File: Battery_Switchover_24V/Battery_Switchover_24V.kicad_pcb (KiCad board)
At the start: 4 copper layers, 198.6 x 89 mm, 186 parts, among them J1 USB_C_Receptacle_USB2.0_14P, J10 ATX_2X3, J11 ATX_2X3, J12 ATX_2X3, J13 ATX_2X3, J2 M8, J4 M8, J5 M8, J6 Conn_01x08, J7 Conn_01x05, J8 ATX_2X3, J9 ATX_2X3, M1 Fan, Q1 PZT2222AT1G, Q10 FDBL86066-F085, Q11 BC817, Q2 PJD50N10AL_L2, Q3 PJD50N10AL_L2, Q4 FDBL86066-F085, Q5 FDBL86066-F085, Q6 FDBL86066-F085, Q7 FDBL86066-F085, Q8 FDBL86066-F085, Q9 FDBL86066-F085, SW1 SW_Push, SW2 SW_Push, SW3 SW_Push, U1 LM25117PSQE_NOPB, U10 LPC11U67JBD48, U12 L5973D, U13 AMS1117-3.3, U14 OPA2197xD, U15 IRS21867S, U16 LM74610QDGKRQ1, U17 IRS21867S, U18 LM60CIM3_NOPB, U2 ACS71240LLCBTR-010B3, U3 IRS21867S, U4 ACS71240LLCBTR-010B3, U5 ACS71240LLCBTR-010B3, U6 LM74610QDGKRQ1, U7 ACS71240LLCBTR-010B3, U8 ADS7830IPWR, U9 LMV321

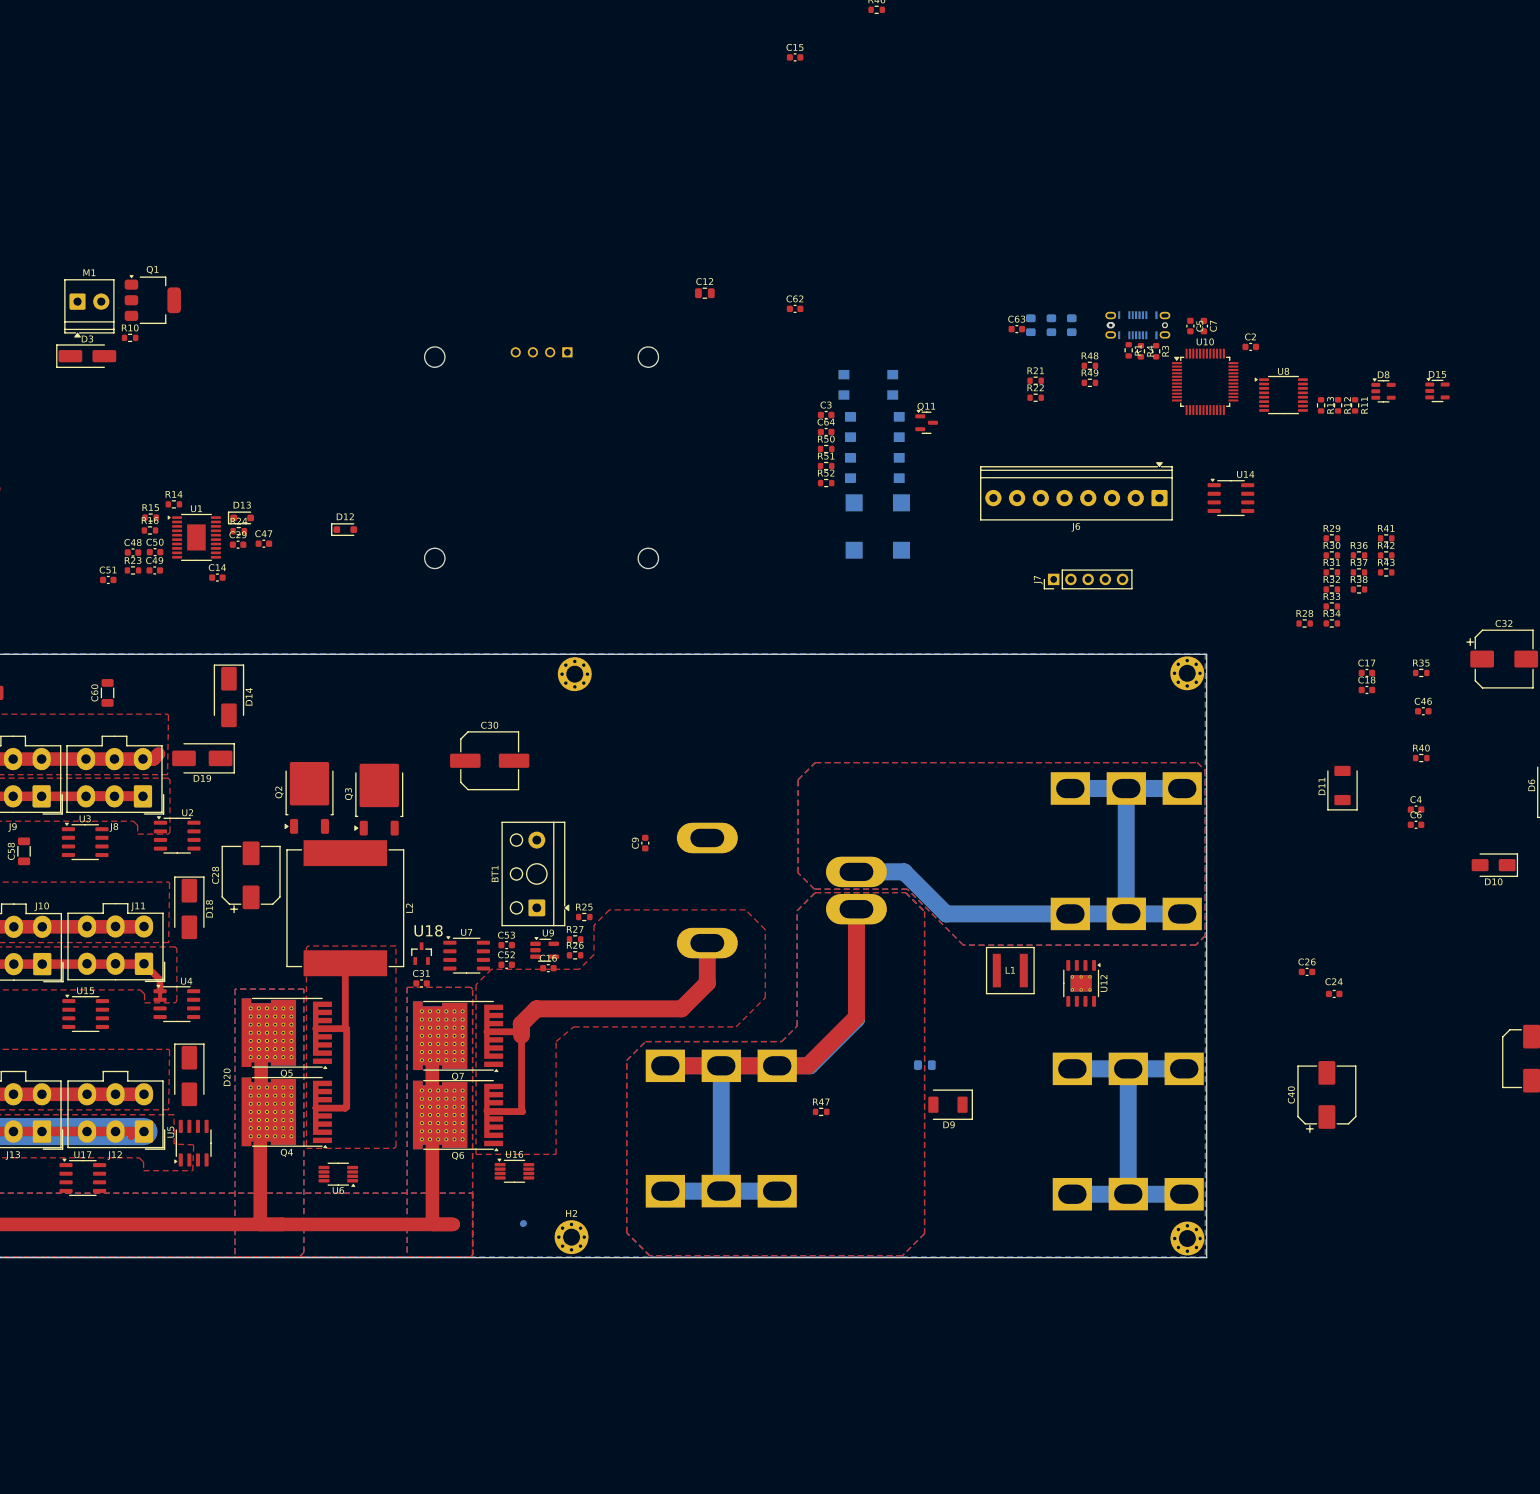
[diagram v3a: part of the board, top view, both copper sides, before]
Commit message: Added batt terminals
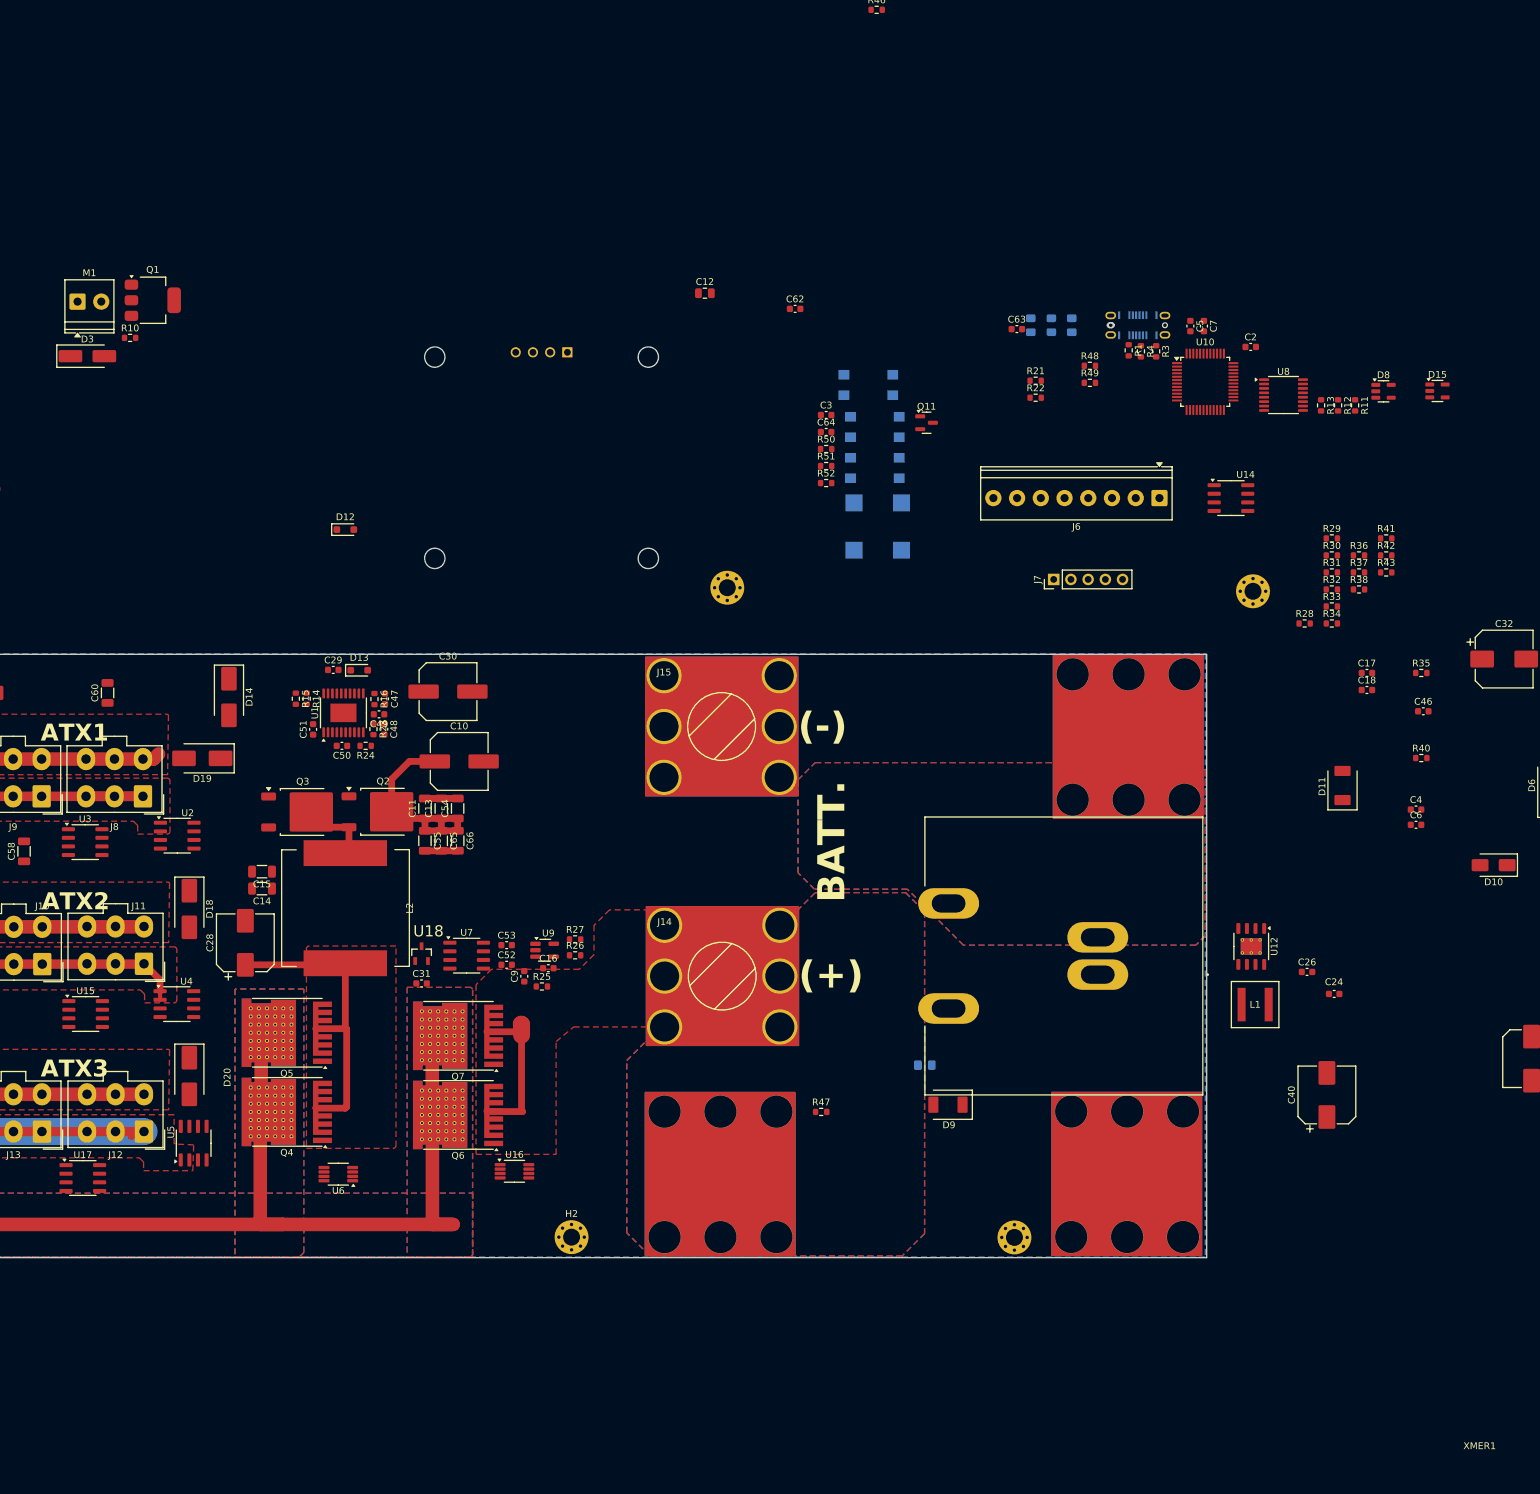
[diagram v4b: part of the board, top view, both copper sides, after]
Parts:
- removed BT1: Battery_Cell, TerminalBlock_RND:TerminalBlock_RND_205-00023_1x02_P10.00mm_Horizontal
- added C10: 330uF, Capacitor_SMD:C_Elec_8x10.2, F.Cu at (177.6, 85.8)
- added C11: 10uF 50V X7R, Capacitor_SMD:C_1206_3216Metric, F.Cu at (172.6, 92.7)
- added C13: 10uF 50V X7R, Capacitor_SMD:C_1206_3216Metric, F.Cu at (175.0, 92.7)
- added C54: 10uF 50V X7R, Capacitor_SMD:C_1206_3216Metric, F.Cu at (177.4, 92.7)
- added C55: 10uF 50V X7R, Capacitor_SMD:C_1206_3216Metric, F.Cu at (172.6, 97.5)
- added C65: 10uF 50V X7R, Capacitor_SMD:C_1206_3216Metric, F.Cu at (174.9, 97.5)
- added C66: 10uF 50V X7R, Capacitor_SMD:C_1206_3216Metric, F.Cu at (177.4, 97.5)
- added J14: M6, M8_Screw_Terminal:M6_Screw_Terminal, F.Cu at (207.9, 110.0)
- added J15: M6, M8_Screw_Terminal:M6_Screw_Terminal, F.Cu at (207.8, 73.2)
- C14: value 100nF -> 10uF; footprint Capacitor_SMD:C_0603_1608Metric -> Capacitor_SMD:C_1206_3216Metric
- C15: footprint Capacitor_SMD:C_0603_1608Metric -> Capacitor_SMD:C_1206_3216Metric
- L2: value L -> 8.2uH 20A
- XMER1: moved to F.Cu
- moved C15 143.6 mm to (148.5, 102.1), turned to 180 degrees
- moved C14 46.3 mm to (148.5, 104.6), turned to 180 degrees
- moved C48 45.3 mm to (166.6, 81.0), turned to -90 degrees
- moved R23 42.5 mm to (164.9, 81.0), turned to -90 degrees
- moved R16 41.4 mm to (165.1, 76.6), turned to -90 degrees
- moved C50 39.7 mm to (160.3, 83.5), turned to 180 degrees
- moved C49 39.3 mm to (165.8, 78.8), turned to 180 degrees
- moved C51 37.4 mm to (156.1, 81.1), turned to 90 degrees
- moved XMER1 36.9 mm to (266.8, 114.5)
- moved R24 36.8 mm to (163.8, 83.5), turned to 180 degrees
- moved L1 36.5 mm to (295.0, 121.7)
- moved R14 34.7 mm to (155.1, 76.5), turned to -90 degrees
- moved R15 34.2 mm to (153.5, 76.5), turned to -90 degrees
- moved U1 33.8 mm to (160.5, 78.6), turned to 90 degrees
- moved C47 29.0 mm to (166.7, 76.6), turned to -90 degrees
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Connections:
- C14 pad 1: VBATT -> Net-(U7-IP+1)
- C15 pad 1: VBATT -> Net-(U7-IP+1)
- C28 pad 1: VBATT -> Net-(U7-IP+1)
- L2 pad 2: VBATT -> Net-(U7-IP+1)
- U7 pad 1: Net-(BT1--) -> Net-(U7-IP+1)
- U7 pad 2: Net-(BT1--) -> Net-(U7-IP+1)
- U7 pad 3: GND -> VBATT
- U7 pad 4: GND -> VBATT
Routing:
- net Net-(D6-A1): track 85.6 -> 0.00 mm
- net Net-(D16-K): track 129.4 -> 51.5 mm
- net VBATT: track 30.5 -> 45.4 mm
- net Net-(Q2-S): track 0.00 -> 10.5 mm
- net GND: track 0.00 -> 9.65 mm
- net VIN: track 59.8 -> 56.7 mm
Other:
- board text added: "(+)"
- board text added: "(-)"
- board text added: "ATX1"
- board text added: "ATX2"
- board text added: "ATX3"
- board text added: "BATT."

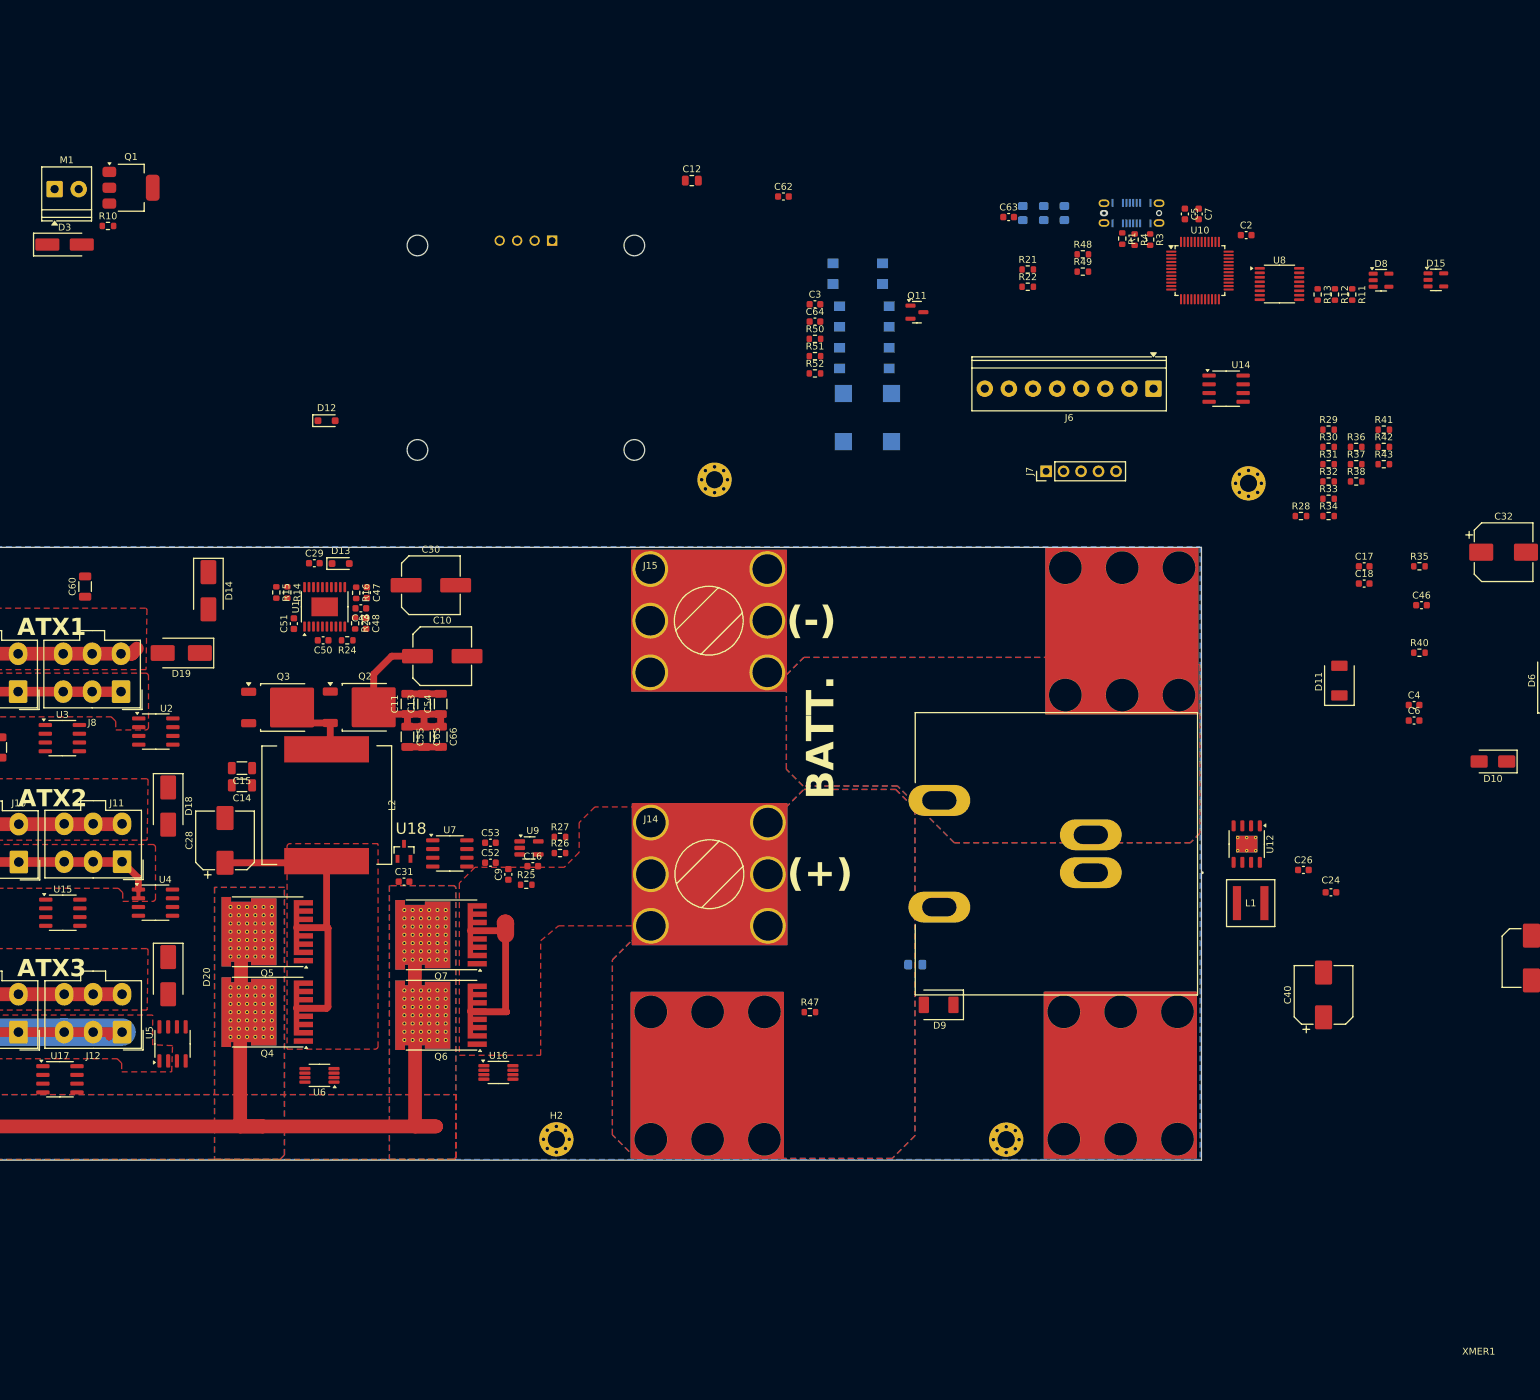
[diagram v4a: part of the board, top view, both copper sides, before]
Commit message: keep outs
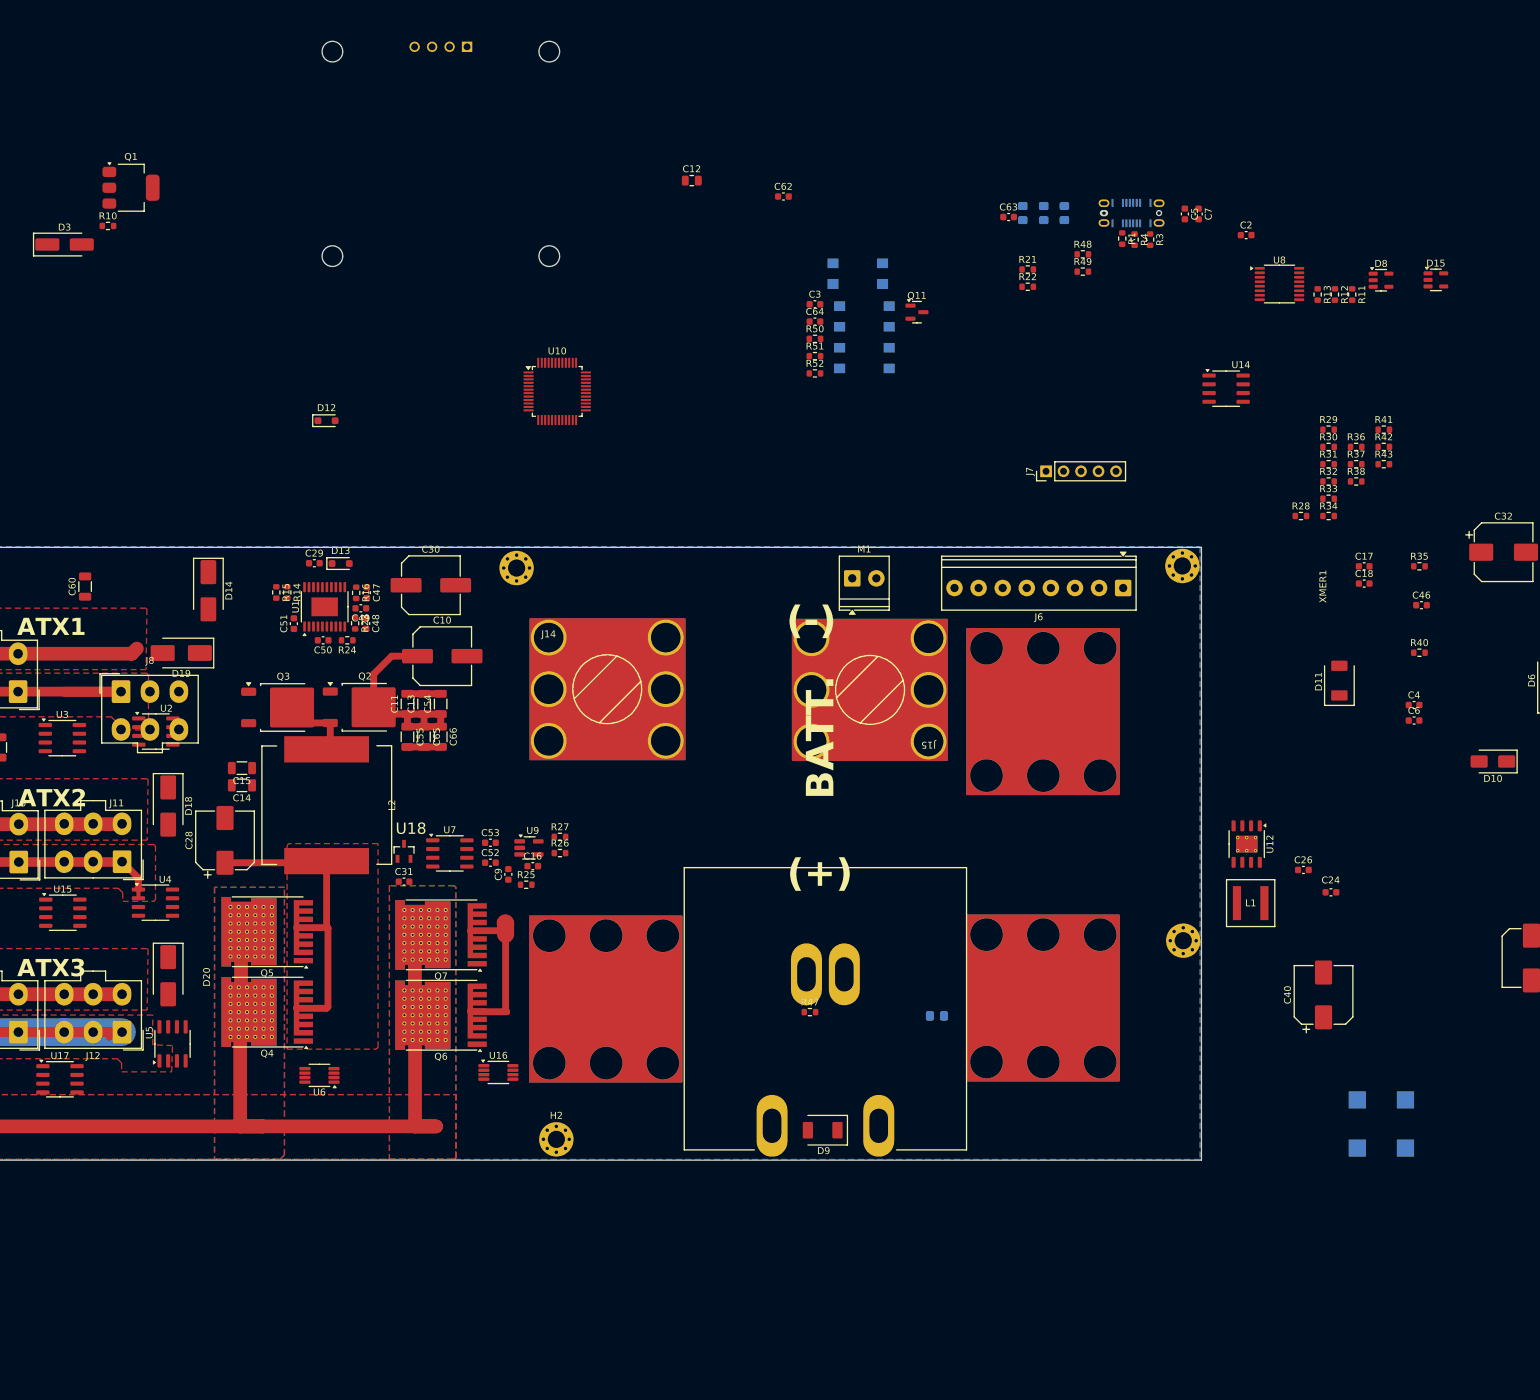
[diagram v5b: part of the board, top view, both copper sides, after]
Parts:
- moved M1 128.9 mm to (237.2, 74.5)
- moved BZ1 126.9 mm to (314.0, 153.8)
- moved U10 95.0 mm to (194.3, 47.4)
- moved J15 47.6 mm to (248.2, 98.2), turned to 180 degrees
- moved XMER1 40.4 mm to (233.2, 137.0), turned to -90 degrees
- moved H5 38.7 mm to (285.2, 127.1)
- moved H6 31.5 mm to (188.4, 73.0)
- moved DS1 30.7 mm to (177.4, 12.8)
- moved J14 30.7 mm to (193.1, 83.1)
- moved J6 29.3 mm to (276.5, 75.9)
- moved D9 24.8 mm to (235.0, 154.7)
- moved J5 18.4 mm to (209.7, 144.9)
- moved J4 16.4 mm to (273.2, 103.2)
- moved J2 15.9 mm to (273.2, 144.8)
- moved H4 15.4 mm to (285.1, 72.7)
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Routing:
- net Net-(D16-A): track 51.5 -> 0.00 mm
- net Net-(D16-K): track 51.5 -> 0.00 mm
- removed copper zone on B.Cu, net Net-(D16-K)
- removed copper zone on F.Cu, net Net-(D16-K)
- removed copper zone on B.Cu, net Net-(D6-A1)
- removed copper zone on F.Cu, net Net-(D6-A1)
- removed copper zone on F.Cu, net VIN
